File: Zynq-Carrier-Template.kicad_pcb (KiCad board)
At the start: 2 copper layers, 49 x 41 mm, 5 parts, among them J1 Zynq_SoM

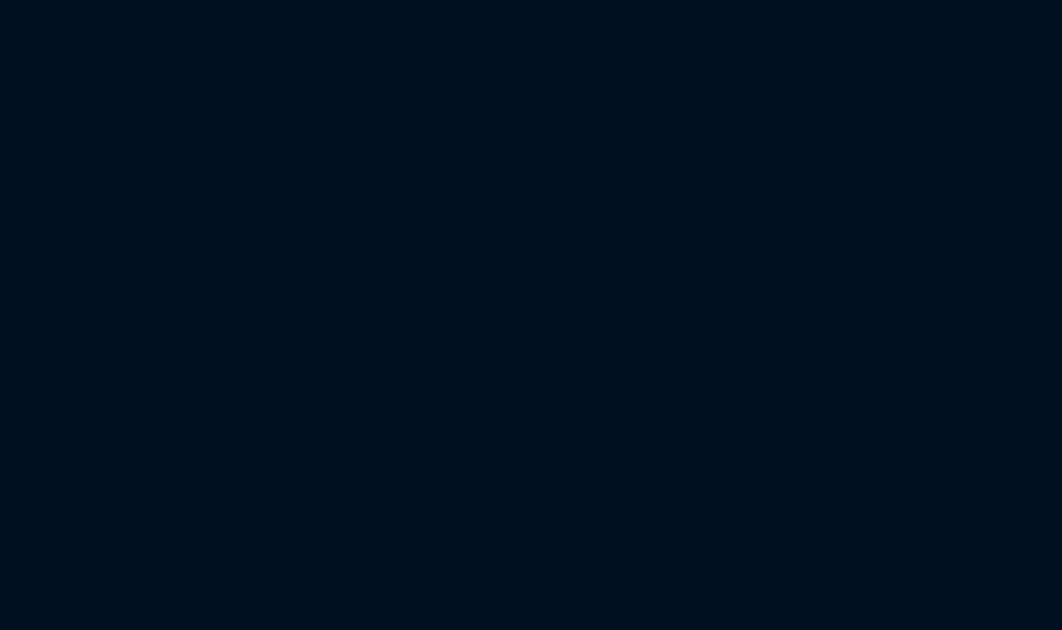
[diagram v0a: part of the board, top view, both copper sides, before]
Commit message: Renamed and Updated Silkscreen
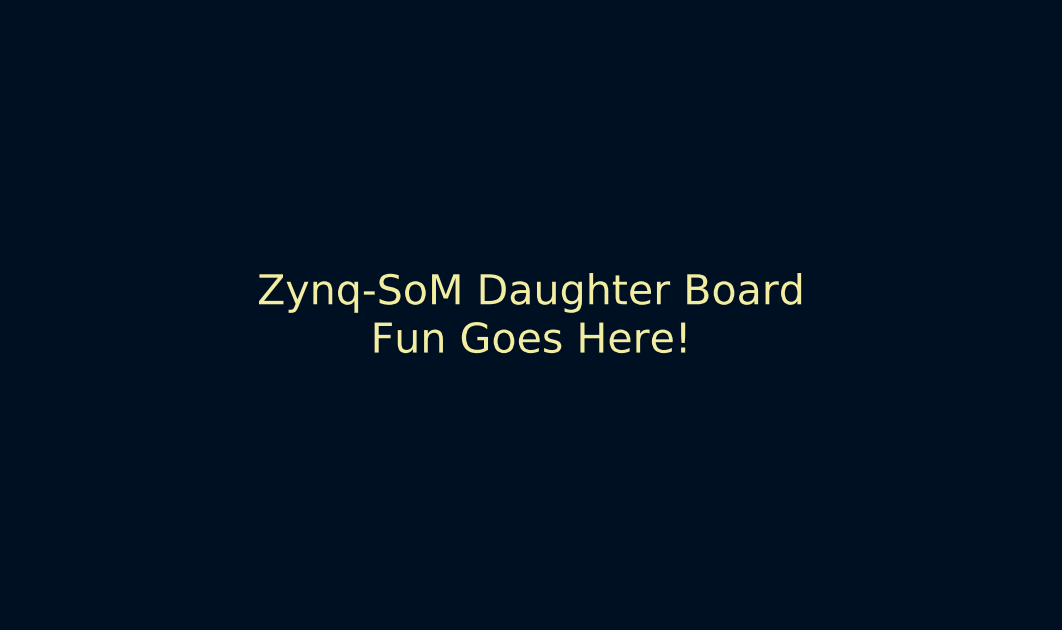
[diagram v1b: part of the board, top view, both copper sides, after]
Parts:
- J1: footprint footprint_Zynq_SoM:Zync_SoM -> footprint_Zynq_SoM:Zynq_SoM
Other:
- board text added: "Zynq-SoM Daughter Board Fun Goes Here!"

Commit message: Squashed commit of the following:
commit 0ad81e69922d32d90721302da68770b5998e2075
Author: pixelatedknight27 <97324570+pixelatedknight27@users.noreply.github.com>
Date:   Wed Aug 6 21:23:02 2025 -0700

    Updated Schematic Switching Regulator Output

commit 8c5282f5a799869a6680777a751af97c305c1966
Author: pixelatedknight27 <maxgross72@gmail.com>
Date:   Wed Jul 30 20:10:45 2025 -0700

    Update Zynq-Carrier-Template.kicad_sch

commit 26cabaedd7311c8d419e12e3f1b26bb927437d1c
Author: pixelatedknight27 <maxgross72@gmail.com>
Date:   Mon Jul 28 15:39:58 2025 -0700

    USB-C Schematic

commit 567233bdd00da02cf27e0d5899afb089722db7fc
Author: eryn-chen <eryncchen@gmail.com>
Date:   Mon Jul 28 14:22:40 2025 -0700

    Import JST_Pins and Inductor

commit 3602218fdc51fd4931fe5a5e7236fe1a478a1e89
Author: pixelatedknight27 <maxgross72@gmail.com>
Date:   Mon Jul 28 13:23:57 2025 -0700

    Added USB-C 3D Model

commit c19733a7ca3310077a98ec0354747d6a3ff68208
Author: eryn-chen <eryncchen@gmail.com>
Date:   Mon Jul 28 12:24:48 2025 -0700

    Import 1uH Inductor

commit dad55b1c15193570489f17efb0b30454465aa197
Author: eryn-chen <eryncchen@gmail.com>
Date:   Sat Jul 26 14:08:40 2025 -0700

    3D Model BQ25629RYKR

commit dfd47739e77adc946db50dcb065d6cd1934a3439
Author: pixelatedknight27 <maxgross72@gmail.com>
Date:   Sat Jul 26 13:56:00 2025 -0700

    Copper Fill demo

commit f9846dcb156c9f426159bf7a8c796c584a4552c7
Author: eryn-chen <eryncchen@gmail.com>
Date:   Sat Jul 26 13:32:59 2025 -0700

    Import BQ25629RYKR

commit 6a2dc9275e746e519794c77d9ef984bae5f9a809
Author: pixelatedknight27 <maxgross72@gmail.com>
Date:   Sat Jul 26 12:43:25 2025 -0700

    Testing collab functionality
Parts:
- added C1: 10uf, Capacitor_SMD:C_0603_1608Metric, F.Cu at (156.7, 109.1)
- added C2: 0.1uf, Capacitor_SMD:C_0603_1608Metric, F.Cu at (163.1, 123.9)
- added C3: 10uf, Capacitor_SMD:C_0603_1608Metric, F.Cu at (163.1, 126.5)
- added C4: 0.1uf, Capacitor_SMD:C_0603_1608Metric, F.Cu at (163.1, 129.0)
- added C5: 10uf, Capacitor_SMD:C_0603_1608Metric, F.Cu at (163.1, 131.5)
- added C6: 0.1uf, Capacitor_SMD:C_0603_1608Metric, F.Cu at (163.1, 134.0)
- added C7: 4.7 uF, Capacitor_SMD:C_0603_1608Metric, F.Cu at (163.5, 139.1)
- added C8: 47 nF, Capacitor_SMD:C_0603_1608Metric, F.Cu at (163.5, 141.6)
- added D1: LED, LED_SMD:LED_0805_2012Metric, F.Cu at (163.4, 136.8)
- added J10: Barrel_Jack_MountingPin, Connector_BarrelJack:BarrelJack_Horizontal, F.Cu at (132.2, 130.6)
- added J2: B2B-PH-K-S, JST_Pins:CONN2_B2B-PH-K-S_JST, F.Cu at (135.7, 103.6)
- added J3: USB_C_Receptacle_USB2.0_16P, Connector_USB:USB_C_Receptacle_G-Switch_GT-USB-7010ASV, F.Cu at (141.2, 112.6)
- added J4: Conn_01x03, Connector_PinHeader_2.54mm:PinHeader_1x03_P2.54mm_Vertical, F.Cu at (117.2, 119.6)
- added J5: Conn_01x03, Connector_PinHeader_2.54mm:PinHeader_1x03_P2.54mm_Vertical, F.Cu at (117.2, 115.6)
- added J6: Conn_01x03, Connector_PinHeader_2.54mm:PinHeader_1x03_P2.54mm_Vertical, F.Cu at (117.2, 123.6)
- added J7: Conn_01x02, Connector_PinHeader_2.54mm:PinHeader_1x02_P2.54mm_Vertical, F.Cu at (117.2, 127.6)
- added J8: Conn_01x02, Connector_PinHeader_2.54mm:PinHeader_1x02_P2.54mm_Vertical, F.Cu at (117.2, 131.6)
- added J9: Conn_01x03, Connector_PinHeader_2.54mm:PinHeader_1x03_P2.54mm_Vertical, F.Cu at (117.2, 111.6)
- added L1: L, Inductor_SMD:L_1008_2520Metric_Pad1.43x2.20mm_HandSolder, F.Cu at (127.2, 115.6)
- added R1: 5.1k, Resistor_SMD:R_0603_1608Metric, F.Cu at (155.4, 117.1)
- added R10: 10K, Resistor_SMD:R_0603_1608Metric, F.Cu at (167.2, 131.5)
- added R2: 5.1k, Resistor_SMD:R_0603_1608Metric, F.Cu at (155.4, 119.6)
- added R3: 5.1k, Resistor_SMD:R_0603_1608Metric, F.Cu at (155.4, 122.1)
- added R4: 1M, Resistor_SMD:R_0603_1608Metric, F.Cu at (155.4, 124.6)
- added R5: 100k, Resistor_SMD:R_0603_1608Metric, F.Cu at (155.4, 100.4)
- added R6: 330, Resistor_SMD:R_0603_1608Metric, F.Cu at (167.2, 121.4)
- added R7: 10K, Resistor_SMD:R_0603_1608Metric, F.Cu at (167.2, 123.9)
- added R8: 4.7k, Resistor_SMD:R_0603_1608Metric, F.Cu at (167.2, 126.5)
- added R9: 4.7k, Resistor_SMD:R_0603_1608Metric, F.Cu at (167.2, 129.0)
- added U1: BQ25629RYKR, BQ25629RYKR:RYK0018A-MFG, F.Cu at (134.2, 110.8)
- added U12: SRV05-4, Package_TO_SOT_SMD:SOT-23-6, F.Cu at (134.1, 114.6)
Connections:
- J1 pad 1: unconnected-(J1A-VIN-Pad1) -> +5V
- J1 pad 10: unconnected-(J1A-VIN-Pad10) -> +5V
- J1 pad 104: unconnected-(J1B-GND-Pad104) -> GND
- J1 pad 105: unconnected-(J1B-GND-Pad105) -> GND
- J1 pad 106: unconnected-(J1B-GND-Pad106) -> GND
- J1 pad 11: unconnected-(J1A-VIN-Pad11) -> +5V
- J1 pad 115: unconnected-(J1B-GND-Pad115) -> GND
- J1 pad 116: unconnected-(J1B-GND-Pad116) -> GND
- J1 pad 12: unconnected-(J1A-VIN-Pad12) -> +5V
- J1 pad 125: unconnected-(J1B-GND-Pad125) -> GND
- J1 pad 126: unconnected-(J1B-GND-Pad126) -> GND
- J1 pad 13: unconnected-(J1A-VIN-Pad13) -> +5V
- J1 pad 135: unconnected-(J1B-GND-Pad135) -> GND
- J1 pad 136: unconnected-(J1B-GND-Pad136) -> GND
- J1 pad 14: unconnected-(J1A-VIN-Pad14) -> +5V
- J1 pad 145: unconnected-(J1B-GND-Pad145) -> GND
- J1 pad 146: unconnected-(J1B-GND-Pad146) -> GND
- J1 pad 15: unconnected-(J1A-GND-Pad15) -> GND
- J1 pad 155: unconnected-(J1B-GND-Pad155) -> GND
- J1 pad 16: unconnected-(J1A-GND-Pad16) -> GND
- J1 pad 165: unconnected-(J1B-GND-Pad165) -> GND
- J1 pad 166: unconnected-(J1B-GND-Pad166) -> GND
- J1 pad 17: unconnected-(J1A-GND-Pad17) -> GND
- J1 pad 175: unconnected-(J1B-GND-Pad175) -> GND
- J1 pad 176: unconnected-(J1B-GND-Pad176) -> GND
- J1 pad 18: unconnected-(J1A-GND-Pad18) -> GND
- J1 pad 185: unconnected-(J1B-GND-Pad185) -> GND
- J1 pad 186: unconnected-(J1B-GND-Pad186) -> GND
- J1 pad 195: unconnected-(J1B-GND-Pad195) -> GND
- J1 pad 196: unconnected-(J1B-GND-Pad196) -> GND
- J1 pad 197: unconnected-(J1B-GND-Pad197) -> GND
- J1 pad 2: unconnected-(J1A-VIN-Pad2) -> +5V
- J1 pad 203: unconnected-(J1C-GND-Pad203) -> GND
- J1 pad 206: unconnected-(J1C-GND-Pad206) -> GND
- J1 pad 213: unconnected-(J1C-GND-Pad213) -> GND
- J1 pad 218: unconnected-(J1C-GND-Pad218) -> GND
- J1 pad 223: unconnected-(J1C-GND-Pad223) -> GND
- J1 pad 228: unconnected-(J1C-GND-Pad228) -> GND
- J1 pad 23: unconnected-(J1A-GND-Pad23) -> GND
- J1 pad 233: unconnected-(J1C-GND-Pad233) -> GND
- J1 pad 238: unconnected-(J1C-GND-Pad238) -> GND
- J1 pad 243: unconnected-(J1C-GND-Pad243) -> GND
- J1 pad 248: unconnected-(J1C-GND-Pad248) -> GND
- J1 pad 253: unconnected-(J1C-GND-Pad253) -> GND
- J1 pad 258: unconnected-(J1C-GND-Pad258) -> GND
- J1 pad 263: unconnected-(J1C-GND-Pad263) -> GND
- J1 pad 268: unconnected-(J1C-GND-Pad268) -> GND
- J1 pad 273: unconnected-(J1C-GND-Pad273) -> GND
- J1 pad 28: unconnected-(J1A-GND-Pad28) -> GND
- J1 pad 280: unconnected-(J1C-GND-Pad280) -> GND
- J1 pad 283: unconnected-(J1C-GND-Pad283) -> GND
- J1 pad 290: unconnected-(J1C-GND-Pad290) -> GND
- J1 pad 295: unconnected-(J1C-GND-Pad295) -> GND
- J1 pad 3: unconnected-(J1A-VIN-Pad3) -> +5V
- J1 pad 30: unconnected-(J1A-USB_D--Pad30) -> /USB_SOM_D-
- J1 pad 300: unconnected-(J1C-GND-Pad300) -> GND
- J1 pad 32: unconnected-(J1A-USB_D+-Pad32) -> /USB_SOM_D+
- J1 pad 39: unconnected-(J1A-GND-Pad39) -> GND
- J1 pad 4: unconnected-(J1A-VIN-Pad4) -> +5V
- J1 pad 44: unconnected-(J1A-GND-Pad44) -> GND
- J1 pad 5: unconnected-(J1A-VIN-Pad5) -> +5V
- J1 pad 51: unconnected-(J1A-GND-Pad51) -> GND
- J1 pad 6: unconnected-(J1A-VIN-Pad6) -> +5V
- J1 pad 62: unconnected-(J1A-GND-Pad62) -> GND
- J1 pad 63: unconnected-(J1A-GND-Pad63) -> GND
- J1 pad 7: unconnected-(J1A-VIN-Pad7) -> +5V
- J1 pad 72: unconnected-(J1A-GND-Pad72) -> GND
- J1 pad 75: unconnected-(J1A-GND-Pad75) -> GND
- J1 pad 8: unconnected-(J1A-VIN-Pad8) -> +5V
- J1 pad 81: unconnected-(J1A-GND-Pad81) -> GND
- J1 pad 82: unconnected-(J1A-GND-Pad82) -> GND
- J1 pad 87: unconnected-(J1A-GND-Pad87) -> GND
- J1 pad 9: unconnected-(J1A-VIN-Pad9) -> +5V
- J1 pad 96: unconnected-(J1A-GND-Pad96) -> GND
- J1 pad 99: unconnected-(J1A-GND-Pad99) -> GND
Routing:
- net /USB_D-: track 0.00 -> 4.01 mm
- net /USB_D+: track 0.00 -> 2.61 mm
- net V_USB: track 0.00 -> 2.24 mm
- net Net-(U1-SW): track 0.00 -> 2.06 mm
- net +5V: vias 0 -> 8
- added copper zone on B.Cu, net +5V
- added copper zone on F.Cu, net +5V
- added copper zone on B.Cu, net GND
- added copper zone on F.Cu, net GND
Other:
- board text removed: "Zynq-SoM Daughter Board Fun Goes Here!"
